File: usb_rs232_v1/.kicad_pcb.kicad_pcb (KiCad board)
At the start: 2 copper layers, 59 x 40 mm, 6 parts, among them CON1 USB-MINI-B, CON2 USB-MICRO-B, IC1 MAX3243, J1 DB9, J2 DB9

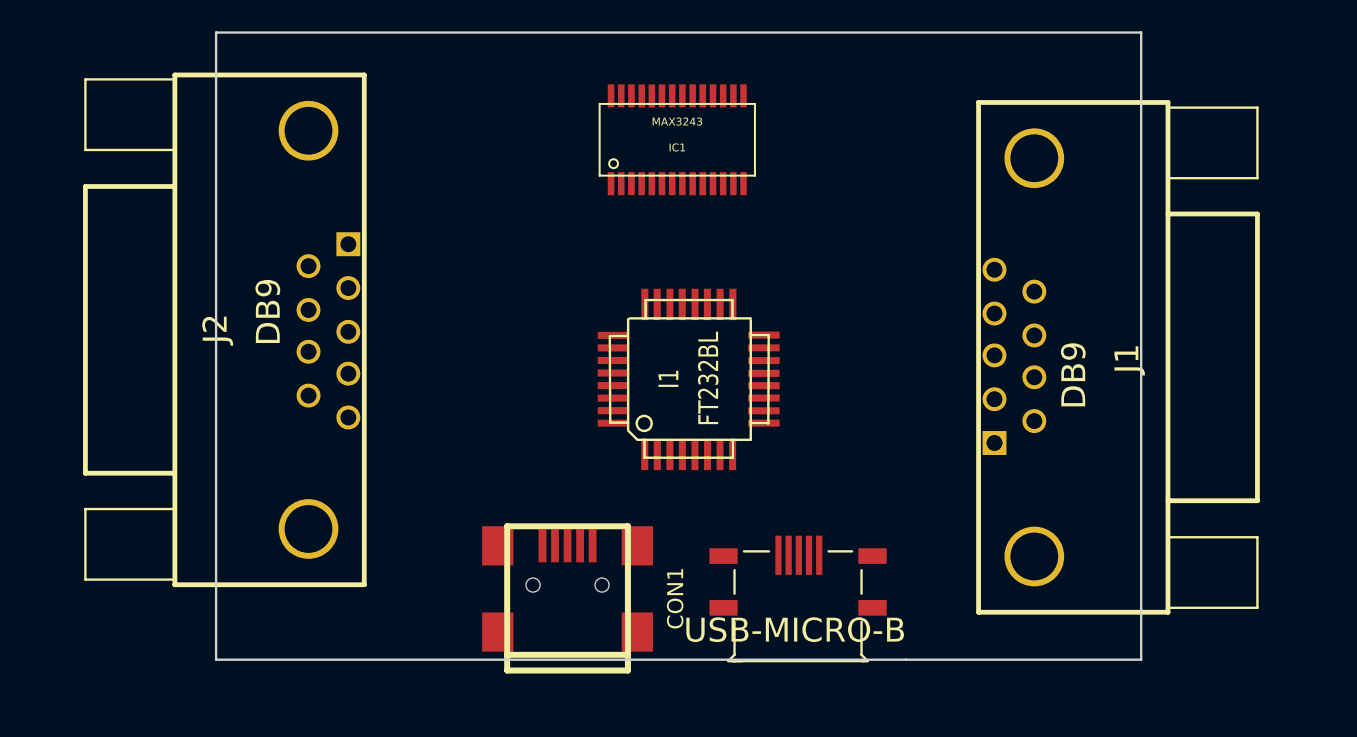
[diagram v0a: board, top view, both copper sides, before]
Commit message: Sprawdzone footprinty
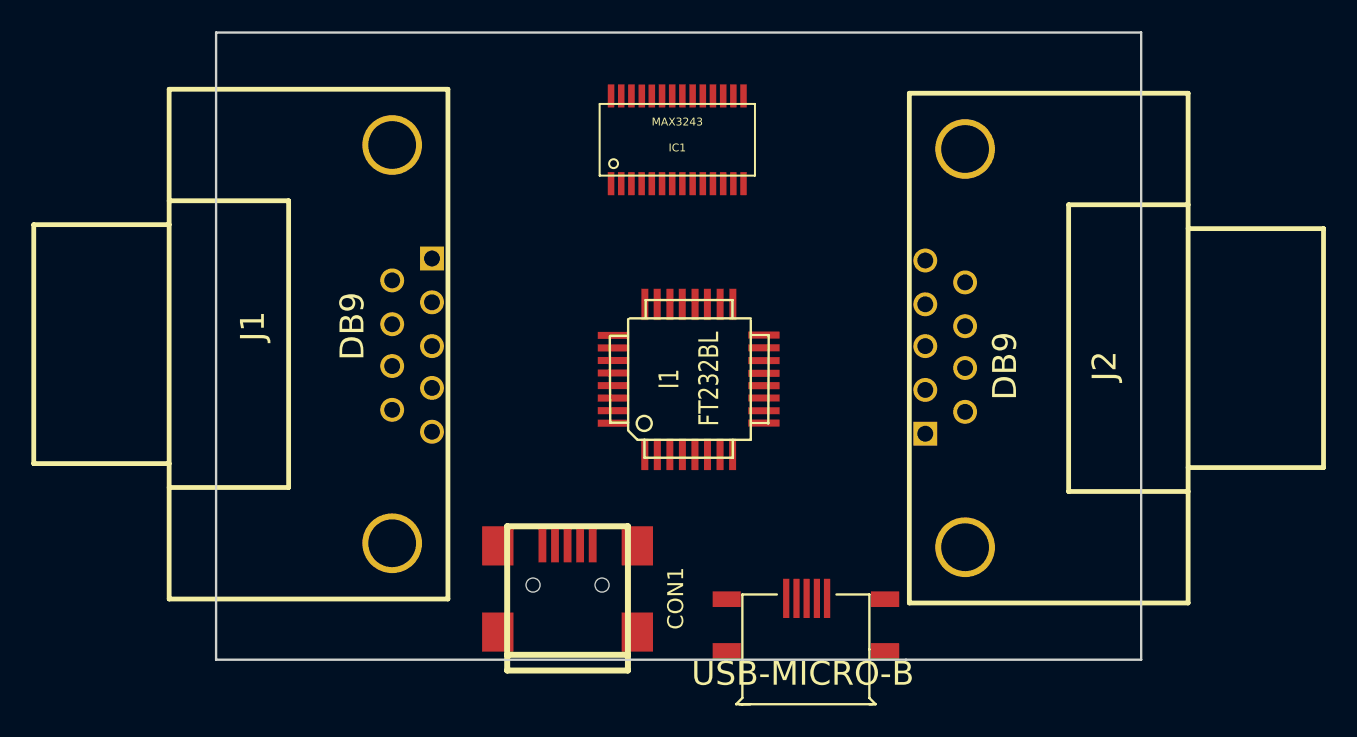
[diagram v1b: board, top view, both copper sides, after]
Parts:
- J1, J2: footprint DB9MC-v2 -> DB9MC
- moved J2 39.3 mm to (121.6, 87.2), turned to 270 degrees
- moved J1 38.4 mm to (87.6, 87.2), turned to 90 degrees
- moved CON2 2.80 mm to (112.8, 106.5)
